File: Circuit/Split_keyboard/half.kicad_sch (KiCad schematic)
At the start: 62 parts, among them SW27 SW_Push, SW28 SW_Push, SW29 SW_Push, SW30 SW_Push, SW31 SW_Push, SW32 SW_Push, SW33 SW_Push, SW34 SW_Push, SW35 SW_Push, SW36 SW_Push, SW37 SW_Push, SW38 SW_Push, SW39 SW_Push, SW40 SW_Push, SW41 SW_Push, SW42 SW_Push, SW43 SW_Push, SW44 SW_Push, SW45 SW_Push, SW46 SW_Push, SW47 SW_Push, SW48 SW_Push, SW49 SW_Push, SW50 SW_Push, SW51 SW_Push, SW52 SW_Push, U2 XIAO-nRF52840-SMD

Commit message: Changed the design of the footprints and maded it simliar to keeb.io keyboards
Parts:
- added D1, D2: D, Diode_SMD:D_SOD-123, symbol Device:D
- added SW1, SW2: SW_Push, marbastlib-choc:SW_choc_v1_HS_CPG135001S30_1u, symbol Switch:SW_Push
- SW27, SW28, SW29, SW30, SW31, SW32, SW33, SW34, SW35, SW36, SW37, SW38, SW39, SW40, SW41, SW42, SW43, SW44, SW45, SW46, SW47, SW48, SW49, SW50, SW51, SW52: footprint marbastlib-choc:SW_choc_v1_1u -> marbastlib-choc:SW_choc_v1_HS_CPG135001S30_1u
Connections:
- net C3: now also SW2.1
- net C4: now also SW1.1
- net R6: now also D1.1 (K), D2.1 (K)
- new net: D1.2 (A), SW1.2
- new net: D2.2 (A), SW2.2
- no-connect marks 0 -> 8

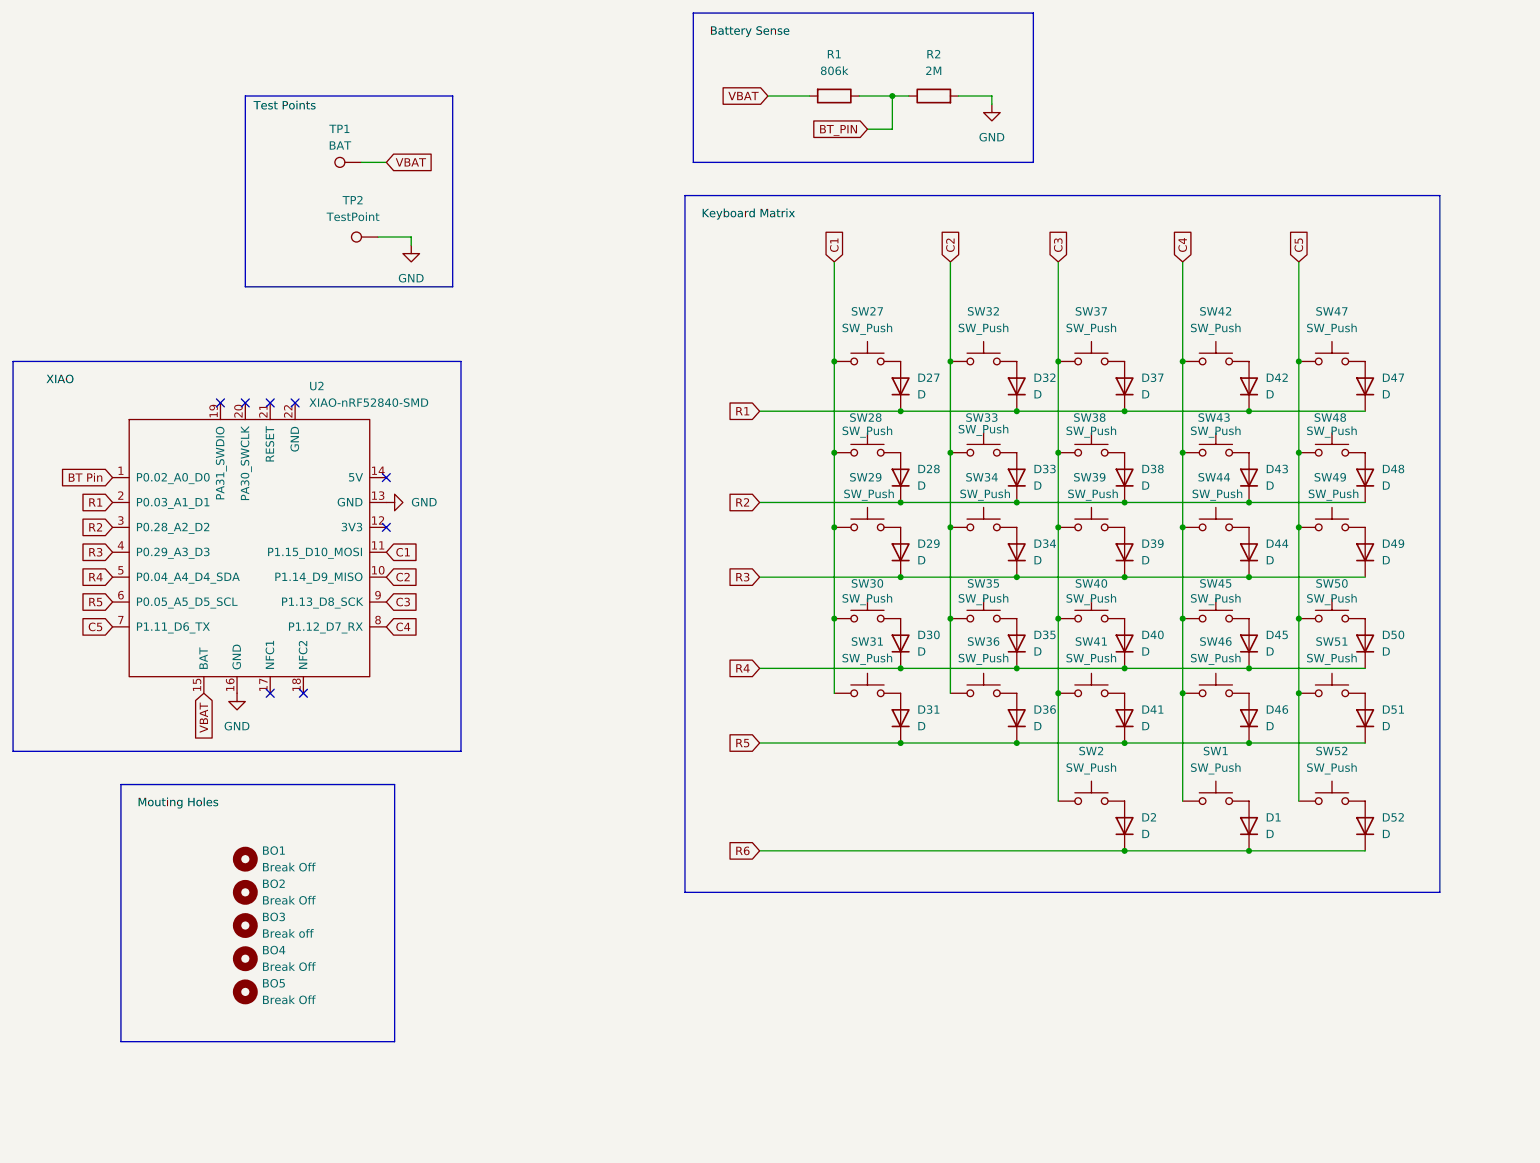
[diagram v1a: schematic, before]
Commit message: Added right side and added edge.cuts for the pcb on both sides
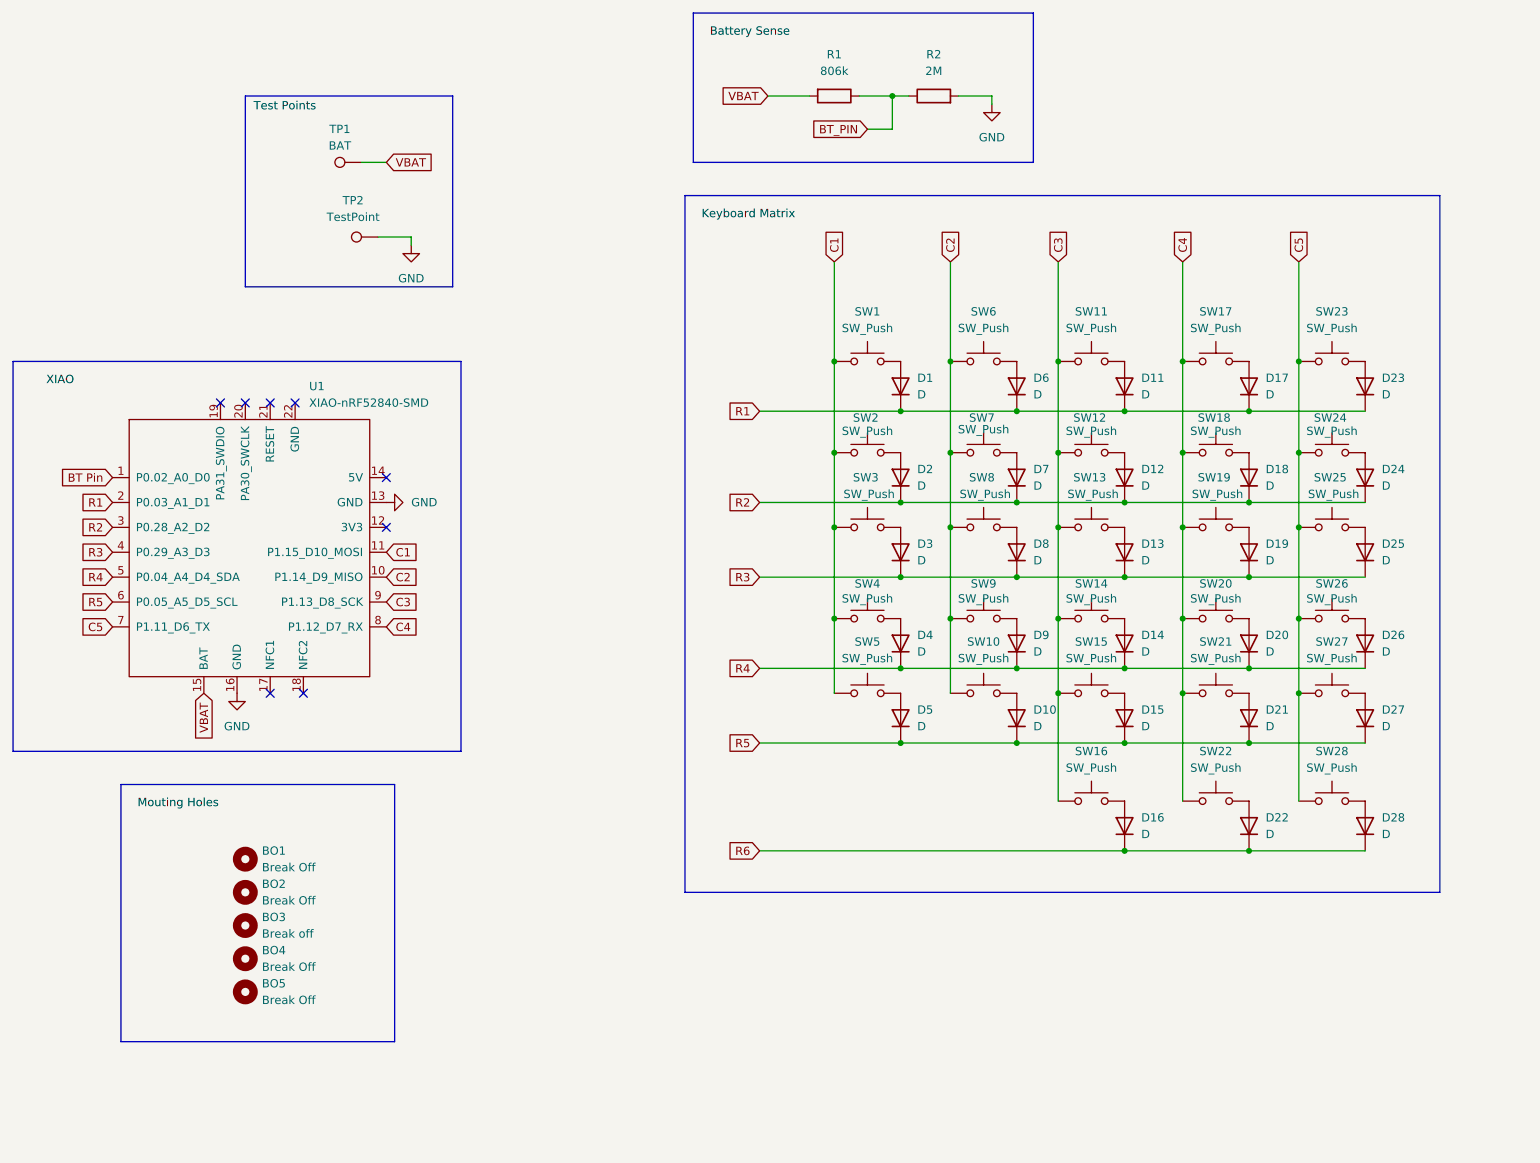
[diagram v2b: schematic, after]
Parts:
- renumbered D27 to D1, D36 to D10, D37 to D11, D38 to D12, D39 to D13, D40 to D14, D41 to D15, D2 to D16, D42 to D17, D43 to D18, D44 to D19, D28 to D2, D45 to D20, D46 to D21, D1 to D22, D47 to D23, D48 to D24, D49 to D25, D50 to D26, D51 to D27, D52 to D28, D29 to D3, D30 to D4, D31 to D5, D32 to D6, D33 to D7, D34 to D8, D35 to D9, SW27 to SW1, SW36 to SW10, SW37 to SW11, SW38 to SW12, SW39 to SW13, SW40 to SW14, SW41 to SW15, SW2 to SW16, SW42 to SW17, SW43 to SW18, SW44 to SW19, SW28 to SW2, SW45 to SW20, SW46 to SW21, SW1 to SW22, SW47 to SW23, SW48 to SW24, SW49 to SW25, SW50 to SW26, SW51 to SW27, SW52 to SW28, SW29 to SW3, SW30 to SW4, SW31 to SW5, SW32 to SW6, SW33 to SW7, SW34 to SW8, SW35 to SW9, U2 to U1

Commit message: Changed the design of the keyboard completelty with schematis
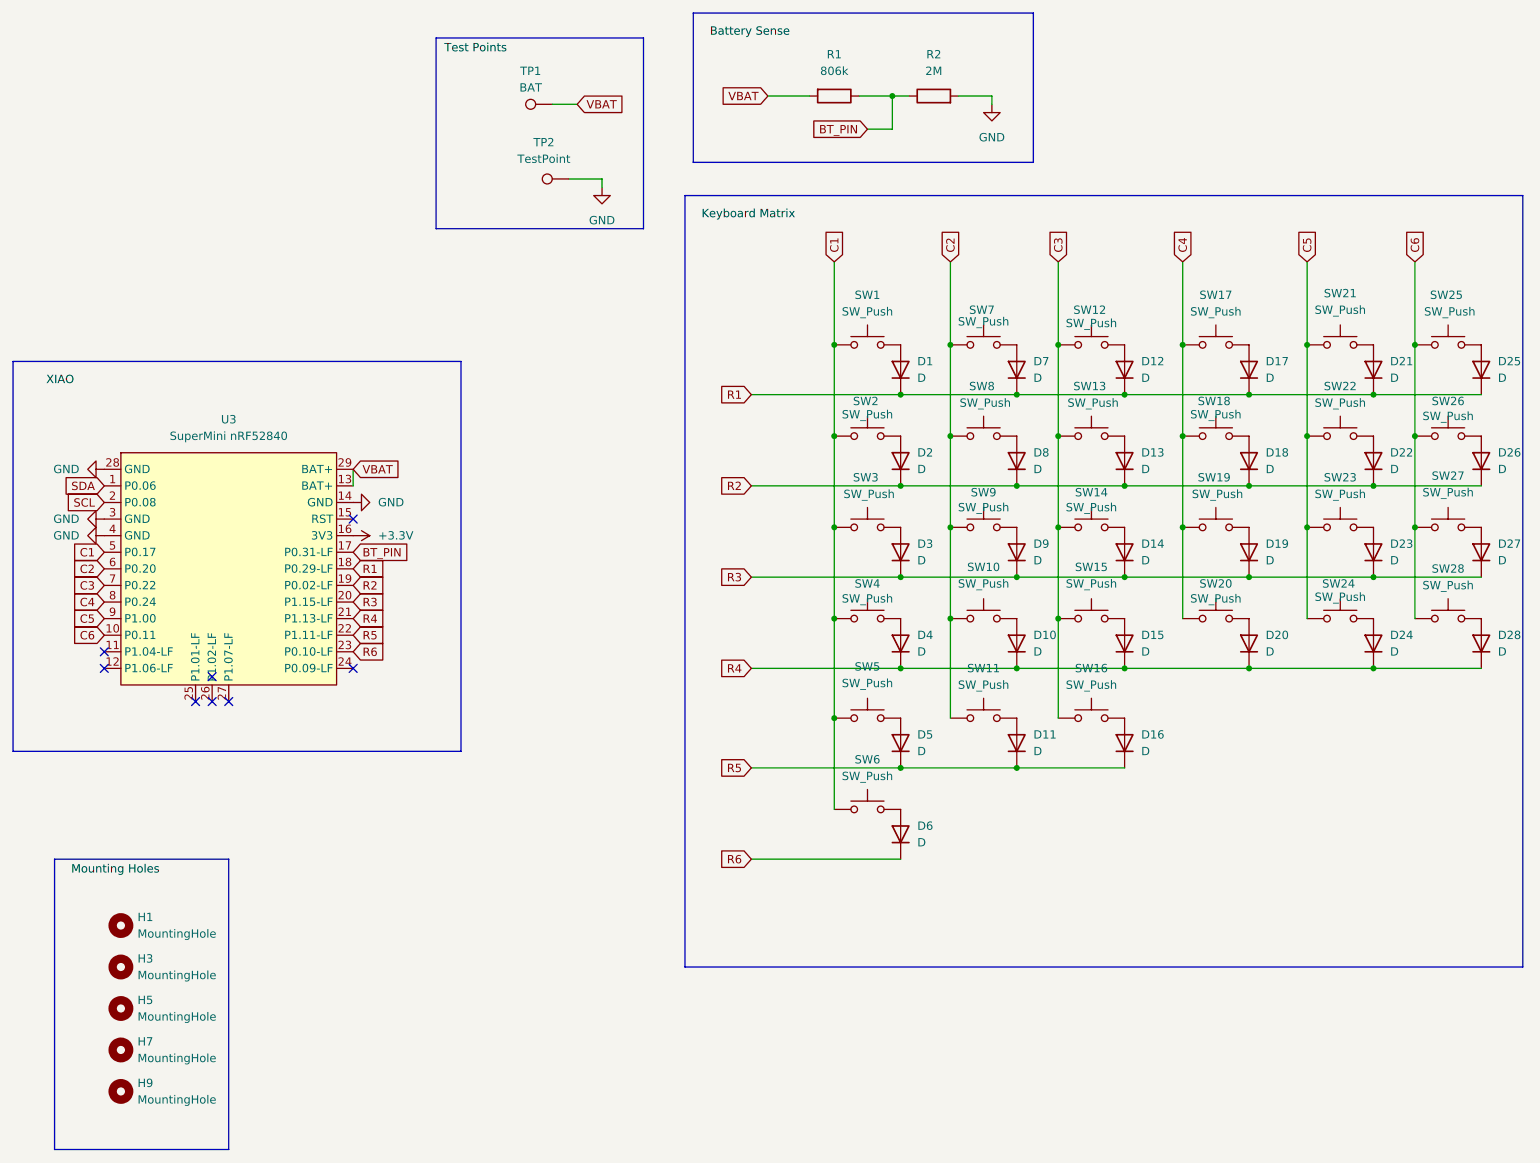
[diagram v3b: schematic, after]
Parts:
- removed BO1, BO2, BO4, BO5: Break Off, Panelization.pretty-master:mouse-bite-5mm-slot, symbol Mechanical:MountingHole
- removed BO3: Break off, Panelization.pretty-master:mouse-bite-5mm-slot, symbol Mechanical:MountingHole
- removed U1: XIAO-nRF52840-SMD, OPL_Kicad:XIAO-nRF52840-SMD, symbol Seeed_Studio_XIAO_Series:XIAO-nRF52840-SMD
- added H1, H3, H5, H7, H9: MountingHole, symbol Mechanical:MountingHole
- added U3: SuperMini nRF52840, PCM_marbastlib-xp-promicroish:SuperMini_nRF52840_AH_USBup, symbol PCM_marbastlib-promicroish:SuperMini_nRF52840
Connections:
- net BT_PIN: now also U3.17 (P0.31-LF)
- net C1: now also SW6.1, U3.5 (P0.17)
- net C2: now also SW11.1, U3.6 (P0.20); no longer SW6.1
- net C3: now also U3.7 (P0.22); no longer SW11.1
- net C4: now also U3.8 (P0.24); no longer SW21.1, SW22.1
- net C5: now also SW21.1, SW22.1, U3.9 (P1.00); no longer SW25.1, SW26.1, SW27.1, SW28.1
- net GND: now also U3.14 (GND), U3.28 (GND), U3.3 (GND), U3.4 (GND)
- net R1: now also D12.1 (K), D21.1 (K), D25.1 (K), D7.1 (K), U3.18 (P0.29-LF); no longer D11.1 (K), D23.1 (K), D6.1 (K)
- net R2: now also D13.1 (K), D22.1 (K), D26.1 (K), D8.1 (K), U3.19 (P0.02-LF); no longer D12.1 (K), D24.1 (K), D7.1 (K)
- net R3: now also D14.1 (K), D23.1 (K), D27.1 (K), D9.1 (K), U3.20 (P1.15-LF); no longer D13.1 (K), D25.1 (K), D8.1 (K)
- net R4: now also D10.1 (K), D15.1 (K), D24.1 (K), D28.1 (K), U3.21 (P1.13-LF); no longer D14.1 (K), D26.1 (K), D9.1 (K)
- net R5: now also D11.1 (K), D16.1 (K), U3.22 (P1.11-LF); no longer D10.1 (K), D15.1 (K), D21.1 (K), D27.1 (K)
- net R6: now also D6.1 (K), U3.23 (P0.10-LF); no longer D16.1 (K), D22.1 (K), D28.1 (K)
- net VBAT: now also U3.13 (BAT+), U3.29 (BAT+)
- new net +3.3V: U3.16 (3V3)
- new net C6: SW25.1, SW26.1, SW27.1, SW28.1, U3.10 (P0.11)
- new net SCL: U3.2 (P0.08)
- new net SDA: U3.1 (P0.06)
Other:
- moved on the sheet: D1, D10, D11, D12, D13, D14, D15, D16, D17, D18, D2, D21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
